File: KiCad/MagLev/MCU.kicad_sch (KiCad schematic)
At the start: 66 parts, among them J2 Programming header, J4 USB_B_Micro, Q1 ZX5T851GTA, Q16 TEMT7000X01, SW1 PTS645, U6 ATmega328P-A, U8 FT232RL, U9 LM1117MP-5.0, Y3 J49SMH-16MHz

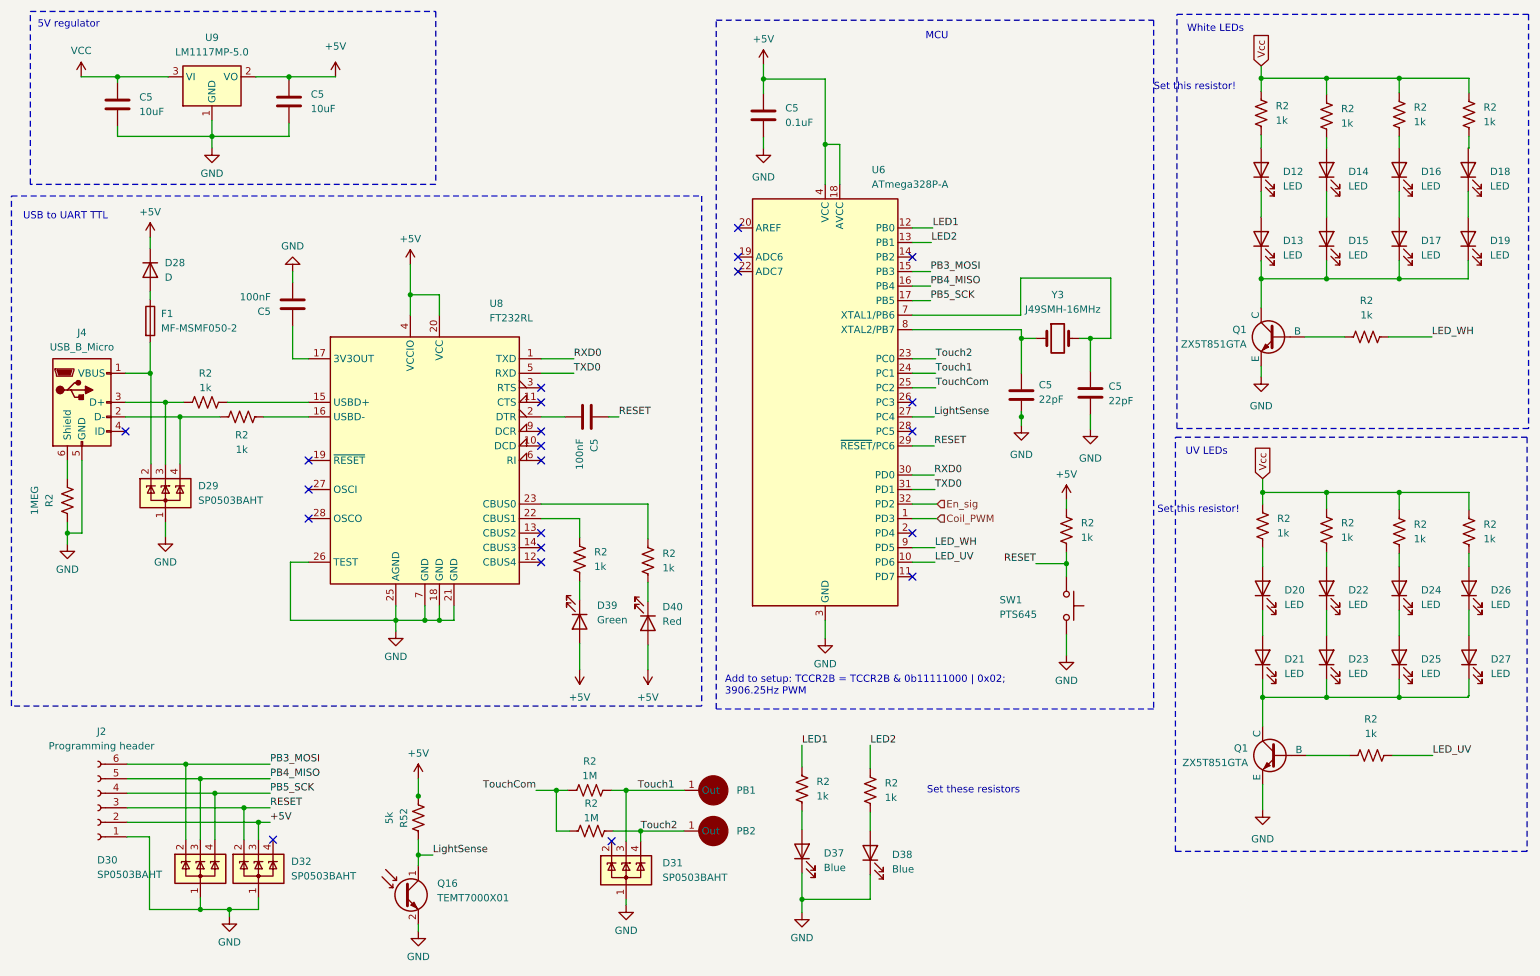
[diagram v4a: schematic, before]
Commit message: Series coils, add TPs.
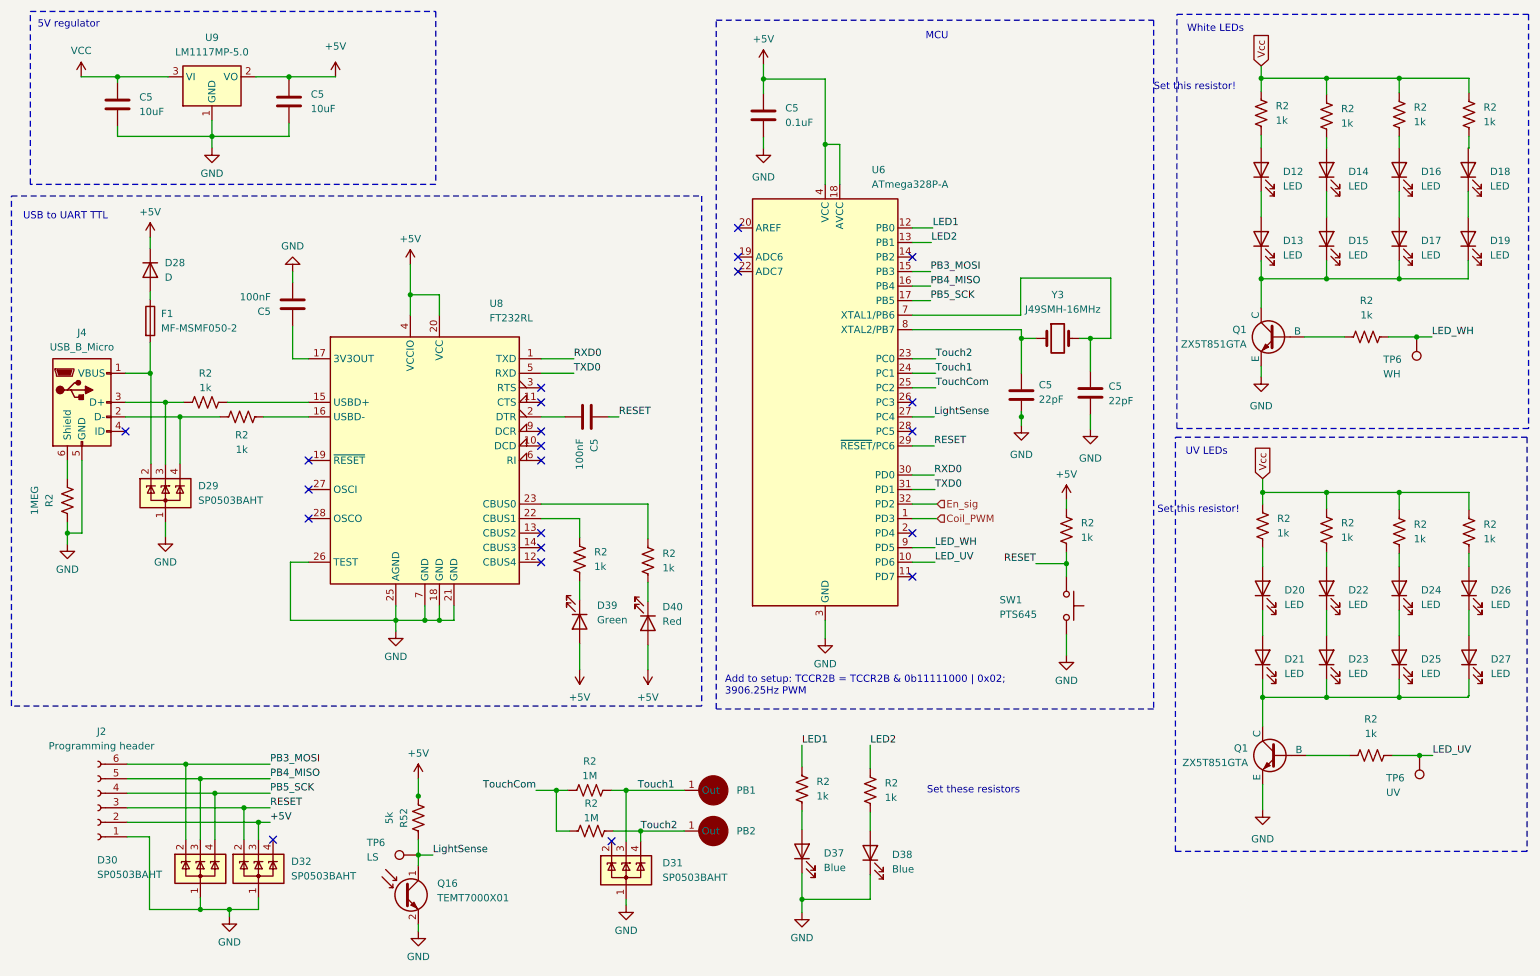
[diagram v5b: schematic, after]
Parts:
- added TP6: LS, TestPoint:TestPoint_Pad_D2.0mm, symbol Connector:TestPoint
- added TP6: WH, TestPoint:TestPoint_Pad_D2.0mm, symbol Connector:TestPoint
- added TP6: UV, TestPoint:TestPoint_Pad_D2.0mm, symbol Connector:TestPoint
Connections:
- net LED_UV: now also TP6.1
- net LED_WH: now also TP6.1
- net LightSense: now also TP6.1
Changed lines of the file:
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@@
   (junction (at 235.712 100.076) (diameter 0) (color 0 0 0 0)
   )
+  (junction (at 263.144 146.05) (diameter 0) (color 0 0 0 0)
+  )
   (junction (at 41.275 79.248) (diameter 0) (color 0 0 0 0)
   )
@@
   )
   (junction (at 201.422 112.522) (diameter 0) (color 0 0 0 0)
+  )
+  (junction (at 262.636 72.898) (diameter 0) (color 0 0 0 0)
   )
   (junction (at 35.56 27.432) (diameter 0) (color 0 0 0 0)
@@
     (stroke (width 0) (type default))
   )
+  (wire (pts (xy 263.144 146.05) (xy 265.43 146.05))
+    (stroke (width 0) (type default))
+  )
   (wire (pts (xy 91.821 122.428) (xy 94.361 122.428))
     (stroke (width 0) (type default))
@@
     (stroke (width 0) (type default))
   )
-  (wire (pts (xy 257.683 72.898) (xy 265.303 72.898))
+  (wire (pts (xy 257.683 72.898) (xy 262.636 72.898))
     (stroke (width 0) (type default))
   )
@@
     (stroke (width 0) (type default))
   )
-  (wire (pts (xy 258.445 146.05) (xy 265.43 146.05))
+  (wire (pts (xy 258.445 146.05) (xy 263.144 146.05))
     (stroke (width 0) (type default))
   )
@@
   )
   (wire (pts (xy 65.786 112.268) (xy 65.786 122.428))
+    (stroke (width 0) (type default))
+  )
+  (wire (pts (xy 262.636 72.898) (xy 265.303 72.898))
     (stroke (width 0) (type default))
   )
@@
         (path "/5eab7e8b-54e1-47d0-9dc3-1e7c3fa2f560/f228425d-6c39-40c9-8e00-a9ebad8217db"
           (reference "#PWR051") (unit 1)
+        )
+      )
+    )
+  )
+  (symbol (lib_id "Connector:TestPoint") (at 88.138 163.449 90) (unit 1)
+    (in_bom yes) (on_board yes) (dnp no)
+    (property "Reference" "TP6" (at 79.121 161.29 90)
+      (effects (font (size 1.27 1.27)) (justify right))
+    )
+    (property "Value" "LS" (at 79.121 163.83 90)
+      (effects (font (size 1.27 1.27)) (justify right))
+    )
+    (property "Footprint" "TestPoint:TestPoint_Pad_D2.0mm" (at 88.138 158.369 0)
+      (effects (font (size 1.27 1.27)) hide)
+    )
+    (property "Datasheet" "~" (at 88.138 158.369 0)
+      (effects (font (size 1.27 1.27)) hide)
+    )
+    (pin "1")
+    (instances
+      (project "MagLev"
+        (path "/5eab7e8b-54e1-47d0-9dc3-1e7c3fa2f560"
+          (reference "TP6") (unit 1)
+        )
+        (path "/5eab7e8b-54e1-47d0-9dc3-1e7c3fa2f560/f228425d-6c39-40c9-8e00-a9ebad8217db"
+          (reference "TP17") (unit 1)
         )
       )
@@
     )
   )
+  (symbol (lib_id "Connector:TestPoint") (at 262.636 72.898 180) (unit 1)
+    (in_bom yes) (on_board yes) (dnp no)
+    (property "Reference" "TP6" (at 256.794 76.835 0)
+      (effects (font (size 1.27 1.27)) (justify right))
+    )
+    (property "Value" "WH" (at 256.794 79.375 0)
+      (effects (font (size 1.27 1.27)) (justify right))
+    )
+    (property "Footprint" "TestPoint:TestPoint_Pad_D2.0mm" (at 257.556 72.898 0)
+      (effects (font (size 1.27 1.27)) hide)
+    )
+    (property "Datasheet" "~" (at 257.556 72.898 0)
+      (effects (font (size 1.27 1.27)) hide)
+    )
+    (pin "1")
+    (instances
+      (project "MagLev"
+        (path "/5eab7e8b-54e1-47d0-9dc3-1e7c3fa2f560"
+          (reference "TP6") (unit 1)
+        )
+        (path "/5eab7e8b-54e1-47d0-9dc3-1e7c3fa2f560/f228425d-6c39-40c9-8e00-a9ebad8217db"
+          (reference "TP19") (unit 1)
+        )
+      )
+    )
+  )
   (symbol (lib_id "Power_Protection:SP0503BAHT") (at 60.198 165.862 0) (unit 1)
     (in_bom yes) (on_board yes) (dnp no) (fields_autoplaced)
@@
         )
       )
+    )
+  )
+  (symbol (lib_id "Connector:TestPoint") (at 263.144 146.05 180) (unit 1)
+    (in_bom yes) (on_board yes) (dnp no)
+    (property "Reference" "TP6" (at 257.302 149.987 0)
+      (effects (font (size 1.27 1.27)) (justify right))
+    )
+    (property "Value" "UV" (at 257.302 152.527 0)
+      (effects (font (size 1.27 1.27)) (justify right))
+    )
+    (property "Footprint" "TestPoint:TestPoint_Pad_D2.0mm" (at 258.064 146.05 0)
+      (effects (font (size 1.27 1.27)) hide)
+    )
+    (property "Datasheet" "~" (at 258.064 146.05 0)
+      (effects (font (size 1.27 1.27)) hide)
+    )
+    (pin "1")
+    (instances
+      (project "MagLev"
+        (path "/5eab7e8b-54e1-47d0-9dc3-1e7c3fa2f560"
+          (reference "TP6") (unit 1)
+        )
+        (path "/5eab7e8b-54e1-47d0-9dc3-1e7c3fa2f560/f228425d-6c39-40c9-8e00-a9ebad8217db"
+          (reference "TP18") (unit 1)
+        )
+      )

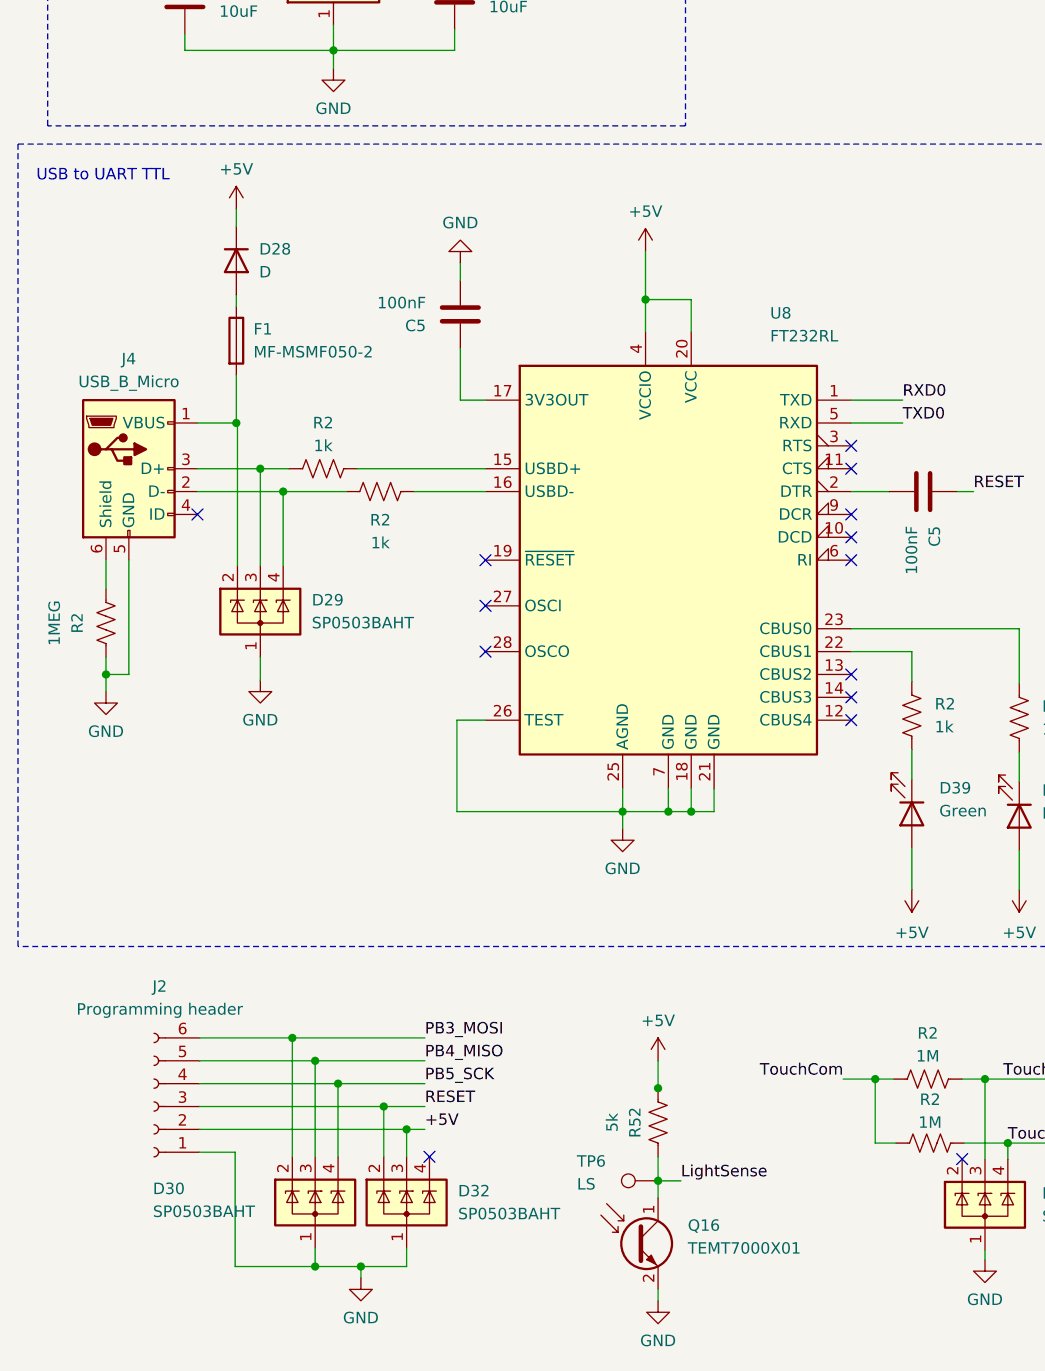
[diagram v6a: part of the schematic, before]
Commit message: Place and route MCU page components.
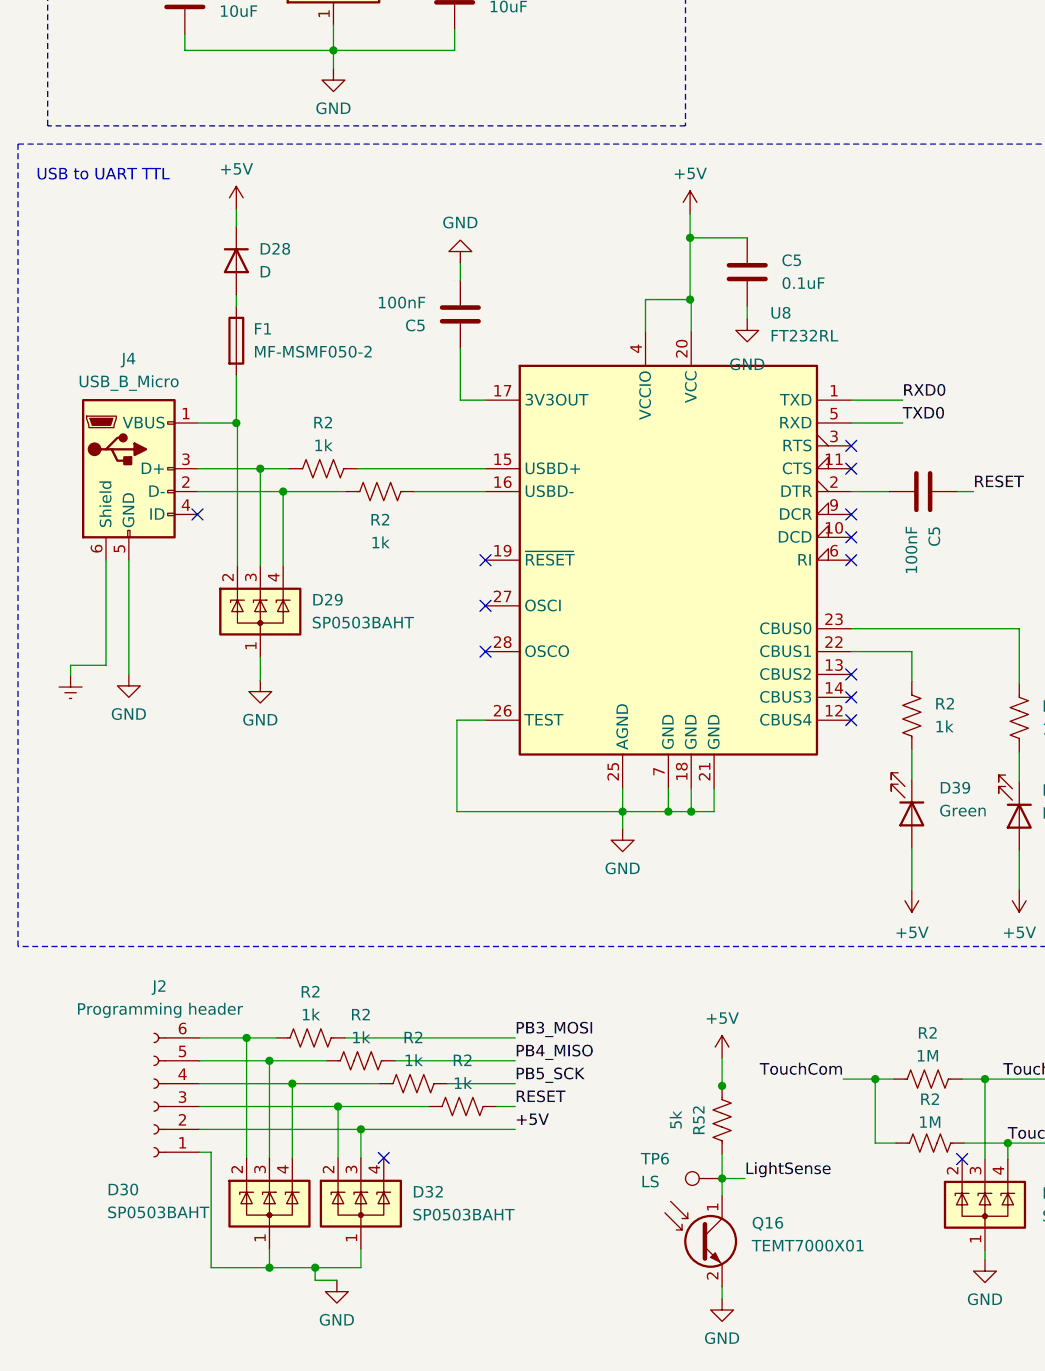
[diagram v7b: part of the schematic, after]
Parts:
- removed R2: 1MEG, Resistor_SMD:R_0805_2012Metric_Pad1.20x1.40mm_HandSolder, symbol Device:R_US
- added C5: 0.1uF, Capacitor_SMD:C_0805_2012Metric_Pad1.18x1.45mm_HandSolder, symbol Device:C
- added R2 (x4): 1k, Resistor_SMD:R_0805_2012Metric_Pad1.20x1.40mm_HandSolder, symbol Device:R_US
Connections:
- net +5V: now also C5.1
- net GND: now also C5.2
- net PB3_MOSI: now also R2.1; no longer D30.2 (K), J2.6 (Pin_6)
- net PB4_MISO: now also R2.1; no longer D30.3 (K), J2.5 (Pin_5)
- net PB5_SCK: now also R2.1; no longer D30.4 (K), J2.4 (Pin_4)
- net RESET: now also R2.1; no longer D32.2 (K), J2.3 (Pin_3)
- net Earth: now reaches J4.6 (Shield)
- new net: D30.4 (K), J2.4 (Pin_4), R2.2
- new net: D32.2 (K), J2.3 (Pin_3), R2.2
- new net: D30.2 (K), J2.6 (Pin_6), R2.2
- new net: D30.3 (K), J2.5 (Pin_5), R2.2
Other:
- moved on the sheet: D30, D32, Q16, R52, TP6

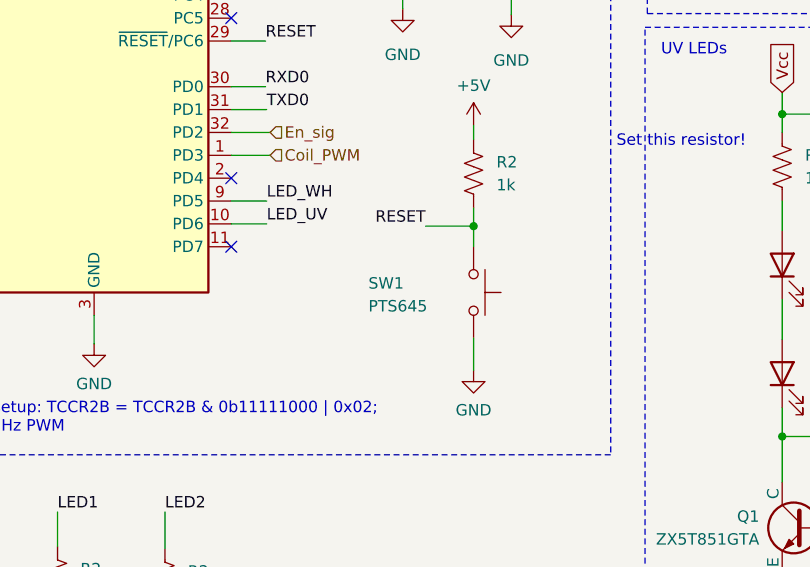
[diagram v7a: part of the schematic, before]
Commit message: Place and route X and Y amplifier components.
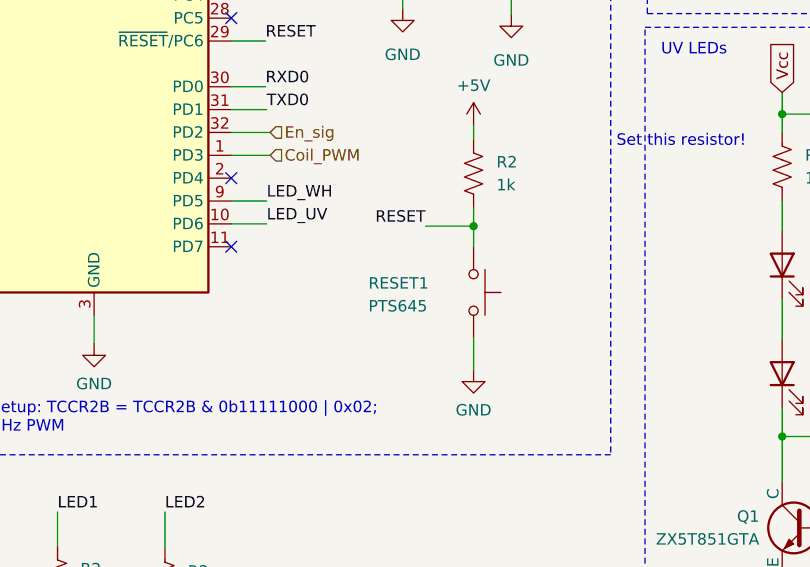
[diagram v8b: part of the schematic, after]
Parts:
- renumbered SW1 to RESET1
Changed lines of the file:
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@@
   (symbol (lib_id "Switch:SW_Push") (at 201.422 119.888 270) (unit 1)
     (in_bom yes) (on_board yes) (dnp no)
-    (property "Reference" "SW1" (at 189.738 118.872 90)
+    (property "Reference" "RESET1" (at 189.738 118.872 90)
       (effects (font (size 1.27 1.27)) (justify left))
     )
@@
       (project "MagLev"
         (path "/5eab7e8b-54e1-47d0-9dc3-1e7c3fa2f560/f228425d-6c39-40c9-8e00-a9ebad8217db"
-          (reference "SW1") (unit 1)
+          (reference "RESET1") (unit 1)
         )
       )
